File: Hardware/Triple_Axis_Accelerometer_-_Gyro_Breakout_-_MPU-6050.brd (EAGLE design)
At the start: 25.4 x 15.2 mm, 20 parts, among them U1 MPU-6050-1, U3 CREATIVE_COMMONS

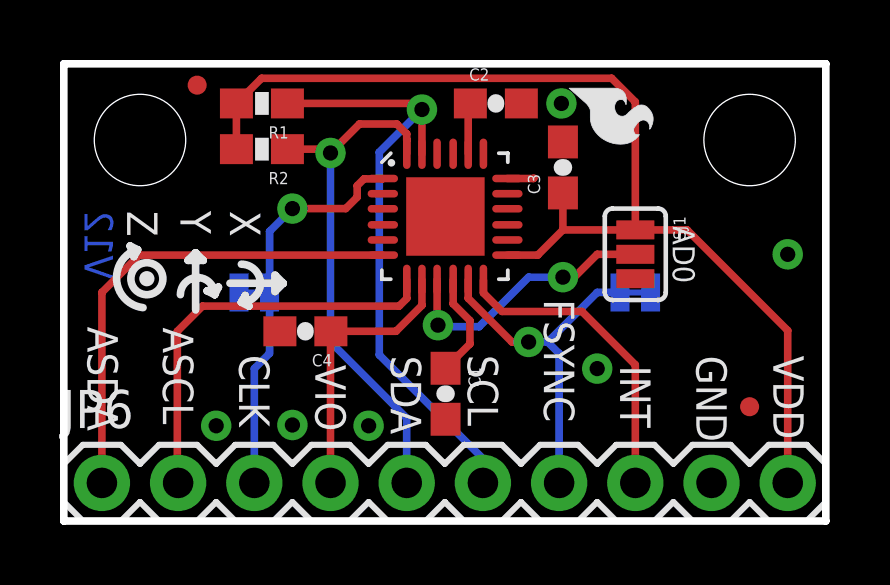
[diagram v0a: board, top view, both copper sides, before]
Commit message: Fixed Air-wire on ADO line
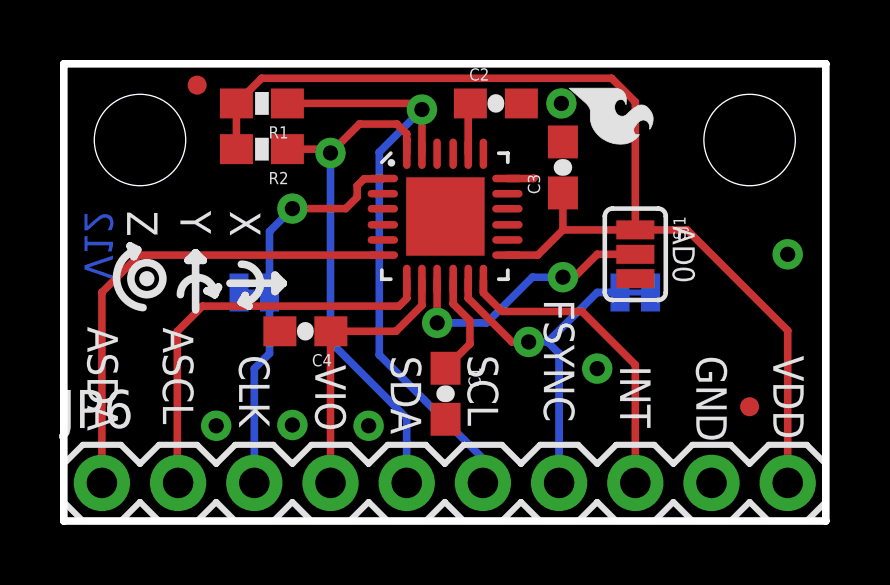
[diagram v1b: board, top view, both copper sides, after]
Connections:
- net N$2 renamed ADO
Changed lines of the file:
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@@
 <setting verticaltext="up"/>
 </settings>
-<grid distance="0.05" unitdist="inch" unit="inch" style="lines" multiple="1" display="yes" altdistance="0.001" altunitdist="inch" altunit="inch"/>
+<grid distance="0.05" unitdist="inch" unit="inch" style="lines" multiple="1" display="yes" altdistance="0.005" altunitdist="inch" altunit="inch"/>
 <layers>
 <layer number="1" name="Top" color="4" fill="1" visible="yes" active="yes"/>
@@
 <wire x1="11.0744" y1="6.3246" x2="8.9018" y2="6.3246" width="0.254" layer="1"/>
 </signal>
-<signal name="N$2">
-<wire x1="12.446" y1="6.477" x2="13.843" y2="6.477" width="0.254" layer="16"/>
-<wire x1="13.843" y1="6.477" x2="15.494" y2="8.128" width="0.254" layer="16"/>
+<signal name="ADO">
 <via x="16.637" y="8.128" extent="1-16" drill="0.508"/>
-<wire x1="15.494" y1="8.128" x2="16.637" y2="8.128" width="0.254" layer="16"/>
 <wire x1="16.637" y1="8.128" x2="17.018" y2="8.128" width="0.254" layer="1"/>
 <wire x1="17.018" y1="8.128" x2="17.78" y2="8.89" width="0.254" layer="1"/>
 <contactref element="U1" pad="9"/>
 <contactref element="SJ1" pad="2"/>
-<via x="12.4714" y="6.5278" extent="1-16" drill="0.508"/>
-<wire x1="12.4425" y1="8.0384" x2="12.4425" y2="6.5567" width="0.254" layer="1"/>
-<wire x1="12.4425" y1="6.5567" x2="12.4714" y2="6.5278" width="0.254" layer="1"/>
 <wire x1="17.78" y1="8.89" x2="19.05" y2="8.89" width="0.254" layer="1"/>
-<wire x1="12.4714" y1="6.5278" x2="12.446" y2="6.477" width="0" layer="19" extent="16-16"/>
+<wire x1="12.4425" y1="8.0384" x2="12.4425" y2="6.6075" width="0.254" layer="1"/>
+<wire x1="12.4425" y1="6.6075" x2="12.446" y2="6.604" width="0.254" layer="1"/>
+<via x="12.446" y="6.604" extent="1-16" drill="0.508"/>
+<wire x1="12.446" y1="6.604" x2="14.097" y2="6.604" width="0.254" layer="16"/>
+<wire x1="14.097" y1="6.604" x2="15.621" y2="8.128" width="0.254" layer="16"/>
+<wire x1="15.621" y1="8.128" x2="16.637" y2="8.128" width="0.254" layer="16"/>
 </signal>
 </signals>
